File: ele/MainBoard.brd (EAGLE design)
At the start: 136.6 x 100 mm, 114 parts, among them IC1 MCP23017SP, IC2 74HC595D, IC3 74HC595D, X1 POWER_IN, X2 POWER_OUT

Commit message: ele: MainBoard - add description texts on PCB
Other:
- board text added: "!SLEEP"
- board text added: "+3V3"
- board text added: "H1"
- board text added: "H2"
- board text added: "H3"
- board text added: "H4"
- board text added: "HREF"
- board text added: "IN1"
- board text added: "IN2"
- board text added: "IN3"
- board text added: "IN4"
- board text added: "LREF"
- board text added: "OUT1"
- board text added: "OUT2"
- board text added: "OUT3"
- board text added: "OUT4"
- board text added: "VCC"
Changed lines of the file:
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@@
 <?xml version="1.0" encoding="utf-8"?>
 <!DOCTYPE eagle SYSTEM "eagle.dtd">
-<eagle version="9.0.1">
+<eagle version="9.0.0">
 <drawing>
 <settings>
@@
 <setting verticaltext="up"/>
 </settings>
-<grid distance="0.025" unitdist="inch" unit="mm" style="lines" multiple="1" display="yes" altdistance="0.01" altunitdist="inch" altunit="mm"/>
+<grid distance="0.025" unitdist="inch" unit="mil" style="lines" multiple="1" display="yes" altdistance="0.01" altunitdist="inch" altunit="mil"/>
 <layers>
 <layer number="1" name="Top" color="4" fill="1" visible="yes" active="yes"/>
@@
 <layer number="16" name="Bottom" color="1" fill="1" visible="yes" active="yes"/>
 <layer number="17" name="Pads" color="2" fill="1" visible="yes" active="yes"/>
-<layer number="18" name="Vias" color="2" fill="1" visible="no" active="yes"/>
+<layer number="18" name="Vias" color="2" fill="1" visible="yes" active="yes"/>
 <layer number="19" name="Unrouted" color="6" fill="1" visible="yes" active="yes"/>
 <layer number="20" name="Dimension" color="24" fill="1" visible="yes" active="yes"/>
@@
 <text x="15.751" y="51.562" size="1.5" layer="51" font="vector" ratio="20" rot="R270">M6</text>
 <text x="13.084" y="51.562" size="1.5" layer="51" font="vector" ratio="20" rot="R270">M5</text>
-<text x="19.688" y="7.239" size="1.5" layer="51" font="vector" ratio="20">IN</text>
+<text x="18.418" y="7.874" size="2.54" layer="51" font="vector" ratio="20">IN</text>
 <text x="12.319" y="95.885" size="1" layer="51" font="vector" ratio="20" rot="R270">SCL</text>
 <text x="2.156" y="23.114" size="1.5" layer="51" font="vector" ratio="20" rot="R90">M1</text>
@@
 <text x="27.559" y="4.445" size="1" layer="51" font="vector" ratio="20" rot="R270" align="bottom-right">GND</text>
 <text x="30.099" y="4.445" size="1" layer="51" font="vector" ratio="20" rot="R270" align="bottom-right">3V3</text>
-<text x="17.783" y="91.059" size="1.5" layer="51" font="vector" ratio="20">OUT</text>
+<text x="26.038" y="89.154" size="2.54" layer="51" font="vector" ratio="20">OUT</text>
 <text x="36.198" y="98.298" size="1.5" layer="51" font="vector" ratio="20">-</text>
 <text x="41.278" y="98.298" size="1.5" layer="51" font="vector" ratio="20">+</text>
@@
 <rectangle x1="45.818621875" y1="94.646221875" x2="46.631421875" y2="94.656378125" layer="21" rot="R90"/>
 <text x="53.975" y="72.39" size="1.4224" layer="21" font="vector" ratio="20" rot="R90">RobotikaBrno.cz</text>
+<text x="33.525" y="1.651" size="1.5" layer="51" font="vector" ratio="20" rot="R180">+</text>
+<text x="46.225" y="1.651" size="1.5" layer="51" font="vector" ratio="20" rot="R180">-</text>
+<text x="32.388" y="98.298" size="1.5" layer="51" font="vector" ratio="20">-</text>
+<text x="45.723" y="98.298" size="1.5" layer="51" font="vector" ratio="20">+</text>
+<text x="49.801" y="40.894" size="1" layer="51" font="vector" ratio="20">EN</text>
+<text x="49.801" y="43.434" size="1" layer="51" font="vector" ratio="20">IN</text>
+<text x="49.801" y="45.974" size="1" layer="51" font="vector" ratio="20">GND</text>
+<text x="49.801" y="48.514" size="1" layer="51" font="vector" ratio="20">OUT</text>
+<text x="128.668" y="30.099" size="1" layer="51" font="vector" ratio="20">EN</text>
+<text x="128.668" y="25.019" size="1" layer="51" font="vector" ratio="20">IN</text>
+<text x="128.668" y="27.559" size="1" layer="51" font="vector" ratio="20">GND</text>
+<text x="128.668" y="22.479" size="1" layer="51" font="vector" ratio="20">OUT</text>
+<text x="128.795" y="75.819" size="1" layer="51" font="vector" ratio="20">EN</text>
+<text x="128.795" y="70.739" size="1" layer="51" font="vector" ratio="20">IN</text>
+<text x="128.795" y="73.279" size="1" layer="51" font="vector" ratio="20">GND</text>
+<text x="128.795" y="68.199" size="1" layer="51" font="vector" ratio="20">OUT</text>
+<text x="41.546" y="12.319" size="1" layer="51" font="vector" ratio="20">IN1</text>
+<text x="41.546" y="14.859" size="1" layer="51" font="vector" ratio="20">IN2</text>
+<text x="41.546" y="17.399" size="1" layer="51" font="vector" ratio="20">VCC</text>
+<text x="41.546" y="19.939" size="1" layer="51" font="vector" ratio="20">GND</text>
+<text x="41.546" y="22.479" size="1" layer="51" font="vector" ratio="20">IN3</text>
+<text x="41.546" y="25.019" size="1" layer="51" font="vector" ratio="20">IN4</text>
+<text x="41.546" y="32.639" size="1" layer="51" font="vector" ratio="20">IN1</text>
+<text x="41.546" y="35.179" size="1" layer="51" font="vector" ratio="20">IN2</text>
+<text x="41.546" y="37.719" size="1" layer="51" font="vector" ratio="20">VCC</text>
+<text x="41.546" y="40.259" size="1" layer="51" font="vector" ratio="20">GND</text>
+<text x="41.546" y="42.799" size="1" layer="51" font="vector" ratio="20">IN3</text>
+<text x="41.546" y="45.339" size="1" layer="51" font="vector" ratio="20">IN4</text>
+<text x="41.546" y="52.959" size="1" layer="51" font="vector" ratio="20">IN1</text>
+<text x="41.546" y="55.499" size="1" layer="51" font="vector" ratio="20">IN2</text>
+<text x="41.546" y="58.039" size="1" layer="51" font="vector" ratio="20">VCC</text>
+<text x="41.546" y="60.579" size="1" layer="51" font="vector" ratio="20">GND</text>
+<text x="41.546" y="63.119" size="1" layer="51" font="vector" ratio="20">IN3</text>
+<text x="41.546" y="65.659" size="1" layer="51" font="vector" ratio="20">IN4</text>
+<text x="41.546" y="73.279" size="1" layer="51" font="vector" ratio="20">IN1</text>
+<text x="41.546" y="75.819" size="1" layer="51" font="vector" ratio="20">IN2</text>
+<text x="41.546" y="78.359" size="1" layer="51" font="vector" ratio="20">VCC</text>
+<text x="41.546" y="80.899" size="1" layer="51" font="vector" ratio="20">GND</text>
+<text x="41.546" y="83.439" size="1" layer="51" font="vector" ratio="20">IN3</text>
+<text x="41.546" y="85.979" size="1" layer="51" font="vector" ratio="20">IN4</text>
+<text x="25.671" y="12.319" size="1" layer="51" font="vector" ratio="20">!FAULT</text>
+<text x="25.671" y="14.859" size="1" layer="51" font="vector" ratio="20">OUT4</text>
+<text x="25.671" y="17.399" size="1" layer="51" font="vector" ratio="20">OUT3</text>
+<text x="25.671" y="19.939" size="1" layer="51" font="vector" ratio="20">OUT2</text>
+<text x="25.671" y="22.479" size="1" layer="51" font="vector" ratio="20">OUT1</text>
+<text x="25.671" y="25.019" size="1" layer="51" font="vector" ratio="20">!SLEEP</text>
+<text x="25.671" y="32.639" size="1" layer="51" font="vector" ratio="20">!FAULT</text>
+<text x="25.671" y="35.179" size="1" layer="51" font="vector" ratio="20">OUT4</text>
+<text x="25.671" y="37.719" size="1" layer="51" font="vector" ratio="20">OUT3</text>
+<text x="25.671" y="40.259" size="1" layer="51" font="vector" ratio="20">OUT2</text>
+<text x="25.671" y="42.799" size="1" layer="51" font="vector" ratio="20">OUT1</text>
+<text x="25.671" y="45.339" size="1" layer="51" font="vector" ratio="20">!SLEEP</text>
+<text x="25.671" y="52.959" size="1" layer="51" font="vector" ratio="20">!FAULT</text>
+<text x="25.671" y="55.499" size="1" layer="51" font="vector" ratio="20">OUT4</text>
+<text x="25.671" y="58.039" size="1" layer="51" font="vector" ratio="20">OUT3</text>
+<text x="25.671" y="60.579" size="1" layer="51" font="vector" ratio="20">OUT2</text>
+<text x="25.671" y="63.119" size="1" layer="51" font="vector" ratio="20">OUT1</text>
+<text x="25.671" y="65.659" size="1" layer="51" font="vector" ratio="20">!SLEEP</text>
+<text x="25.671" y="73.279" size="1" layer="51" font="vector" ratio="20">!FAULT</text>
+<text x="25.671" y="75.819" size="1" layer="51" font="vector" ratio="20">OUT4</text>
+<text x="25.671" y="78.359" size="1" layer="51" font="vector" ratio="20">OUT3</text>
+<text x="25.671" y="80.899" size="1" layer="51" font="vector" ratio="20">OUT2</text>
+<text x="25.671" y="83.439" size="1" layer="51" font="vector" ratio="20">OUT1</text>
+<text x="25.671" y="85.979" size="1" layer="51" font="vector" ratio="20">!SLEEP</text>
+<text x="89.298" y="33.02" size="1" layer="51" font="vector" ratio="20">H1</text>
+<text x="89.298" y="35.56" size="1" layer="51" font="vector" ratio="20">H2</text>
+<text x="89.298" y="38.1" size="1" layer="51" font="vector" ratio="20">HREF</text>
+<text x="89.298" y="40.64" size="1" layer="51" font="vector" ratio="20">GND</text>
+<text x="89.298" y="43.18" size="1" layer="51" font="vector" ratio="20">H3</text>
+<text x="89.298" y="45.72" size="1" layer="51" font="vector" ratio="20">H4</text>
+<text x="96.283" y="33.02" size="1" layer="51" font="vector" ratio="20" align="bottom-right">L1</text>
+<text x="96.283" y="35.56" size="1" layer="51" font="vector" ratio="20" align="bottom-right">L2</text>
+<text x="96.283" y="38.1" size="1" layer="51" font="vector" ratio="20" align="bottom-right">LREF</text>
+<text x="96.283" y="40.64" size="1" layer="51" font="vector" ratio="20" align="bottom-right">GND</text>
+<text x="96.283" y="43.18" size="1" layer="51" font="vector" ratio="20" align="bottom-right">L3</text>
+<text x="96.283" y="45.72" size="1" layer="51" font="vector" ratio="20" align="bottom-right">L4</text>
+<text x="52.708" y="98.298" size="1.5" layer="51" font="vector" ratio="20">-</text>
+<text x="111.128" y="98.298" size="1.5" layer="51" font="vector" ratio="20">-</text>
+<text x="102.873" y="98.298" size="1.5" layer="51" font="vector" ratio="20">+3V3</text>
 </plain>
 <attributes>
@@
 <vertex x="46.99" y="7.62"/>
 </polygon>
+<wire x1="41.91" y1="93.599" x2="39.23" y2="78.74" width="0" layer="19" extent="1-1"/>
+<wire x1="39.23" y1="17.78" x2="36.83" y2="5.461" width="0" layer="19" extent="1-1"/>
+<wire x1="39.23" y1="38.1" x2="53.975" y2="43.815" width="0" layer="19" extent="1-1"/>
+<wire x1="39.23" y1="58.42" x2="39.23" y2="78.74" width="0" layer="19" extent="1-1"/>
 </signal>
 <signal name="EN">

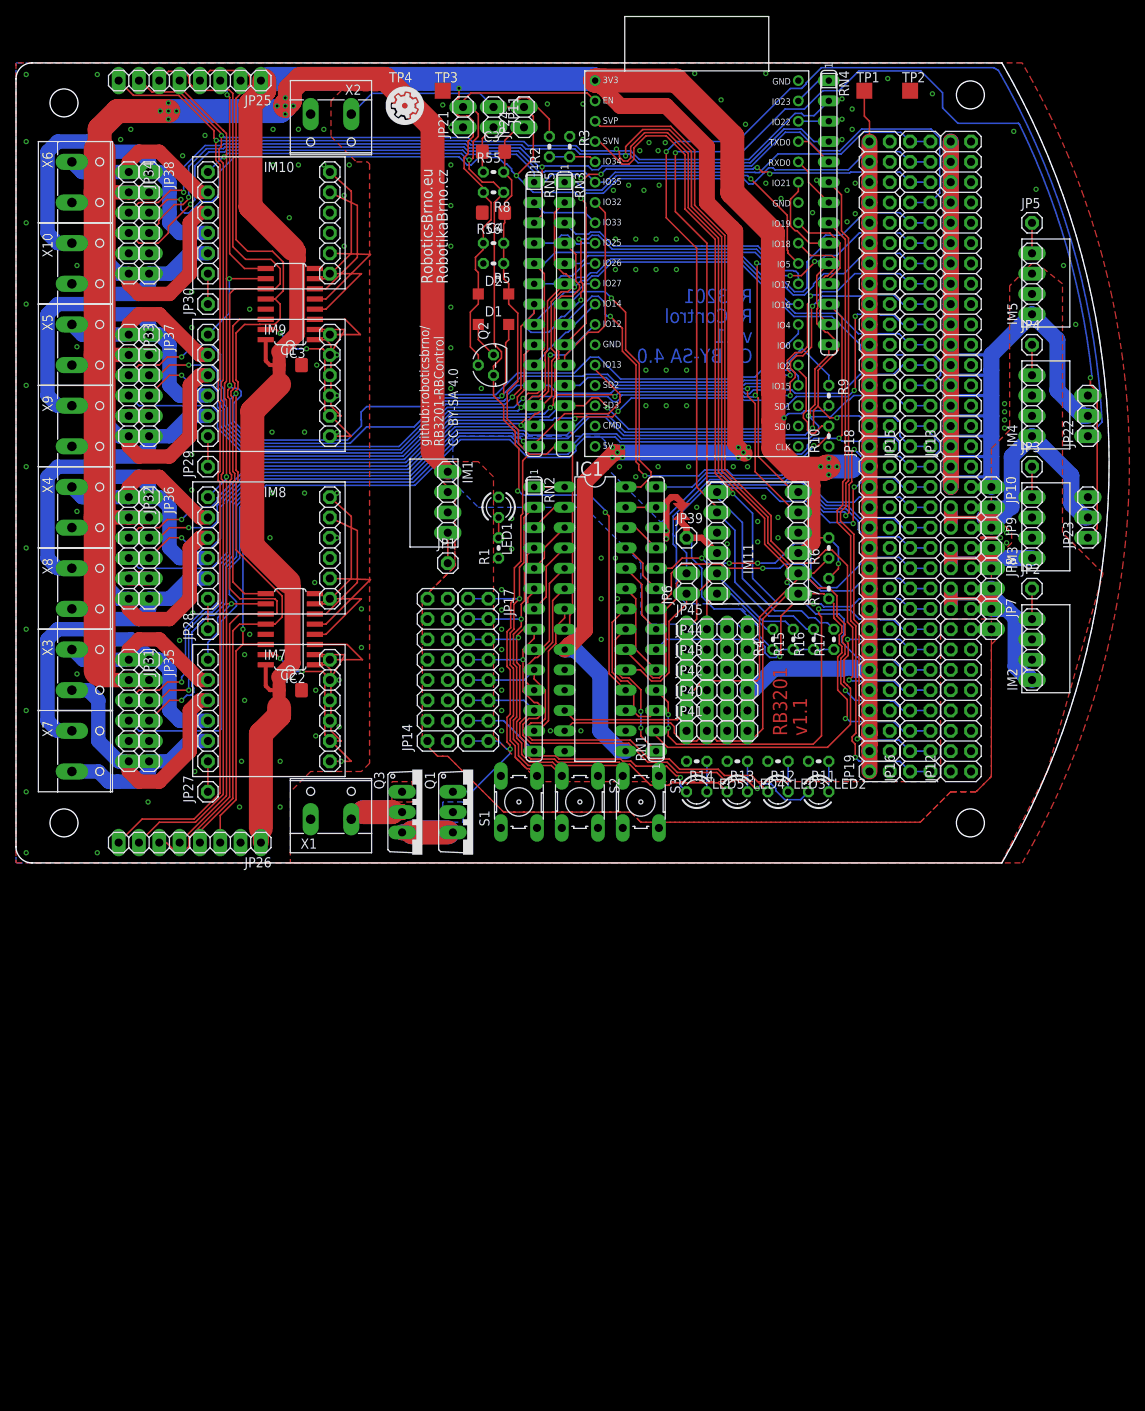
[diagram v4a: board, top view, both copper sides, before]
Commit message: ele: move power switch from GND to VCC (schematic only)
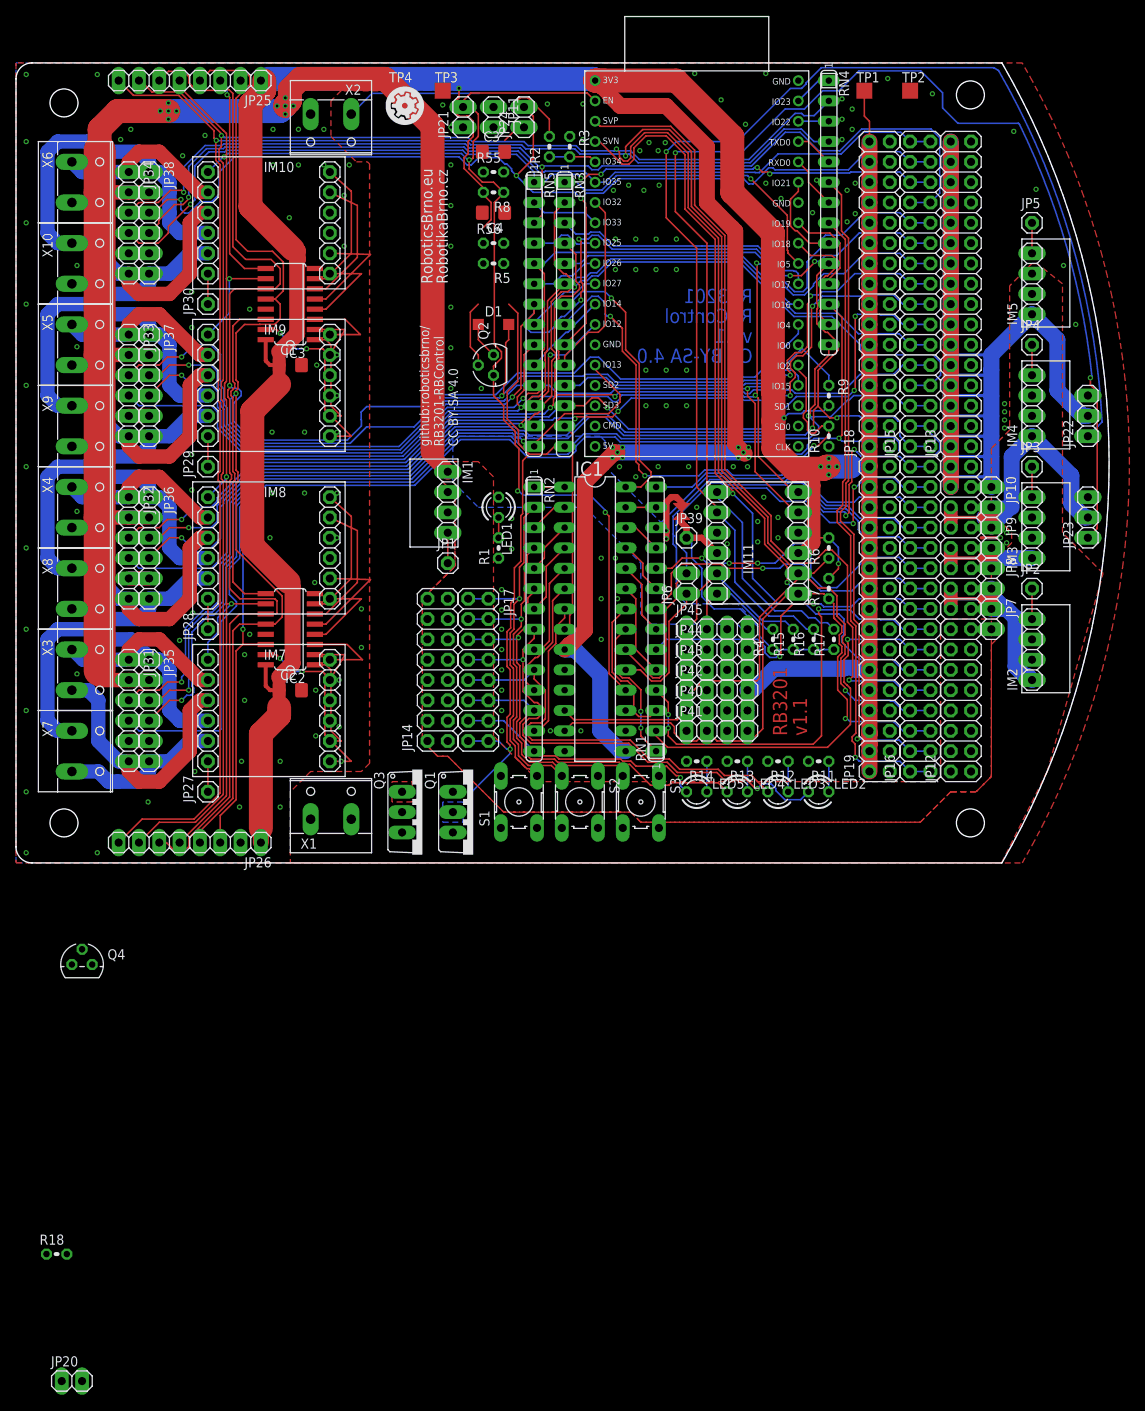
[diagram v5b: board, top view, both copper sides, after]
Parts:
- removed D2: (no value), diode:SOD123
- added JP20: STOP_BUTTON, pinhead:1X02
- added Q4: (no value), transistors:TO92
- added R18: 2M, rcl_upravena:0204V
- JP11: value POWER_BUTTON -> START_BUTTON
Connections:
- removed net BATT_CATHODE: Q3.2, X1.2
- removed net BATT_CATHODE2: Q1.3, Q3.3
- removed net N$19: C3.1, JP11.2, R55.1
- new net BAT: Q3.2, X1.1
- new net BAT_PROT: Q1.3, Q3.3, R5.1
- new net N$1: C3.1, Q1.1, Q4.3, R18.1, R5.2
- new net N$6: C3.2, JP11.1, R18.2
- net +3V3: no longer D2.C
- net ESP_!SHUTDOWN: now also JP20.1, Q4.2, R55.1; no longer C3.2, D2.A, Q1.1, R5.1, R55.2
- net GND: now also JP11.2, JP20.2, Q3.1, Q4.1, R55.2, X1.2; no longer Q1.2, R5.2
- net VCC: now also Q1.2; no longer JP11.1, Q3.1, X1.1
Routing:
- net ESP_!SHUTDOWN: track 104.3 -> 80.4 mm
- net BATT_CATHODE: track 13.4 -> 0.00 mm
- net BATT_CATHODE2: track 12.7 -> 0.00 mm
- net +3V3: track 543.4 -> 533.2 mm
- net N$19: track 6.22 -> 0.00 mm
- net VCC: track 30.3 -> 25.7 mm

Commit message: ele: Fix layout on left side (motor drivers)
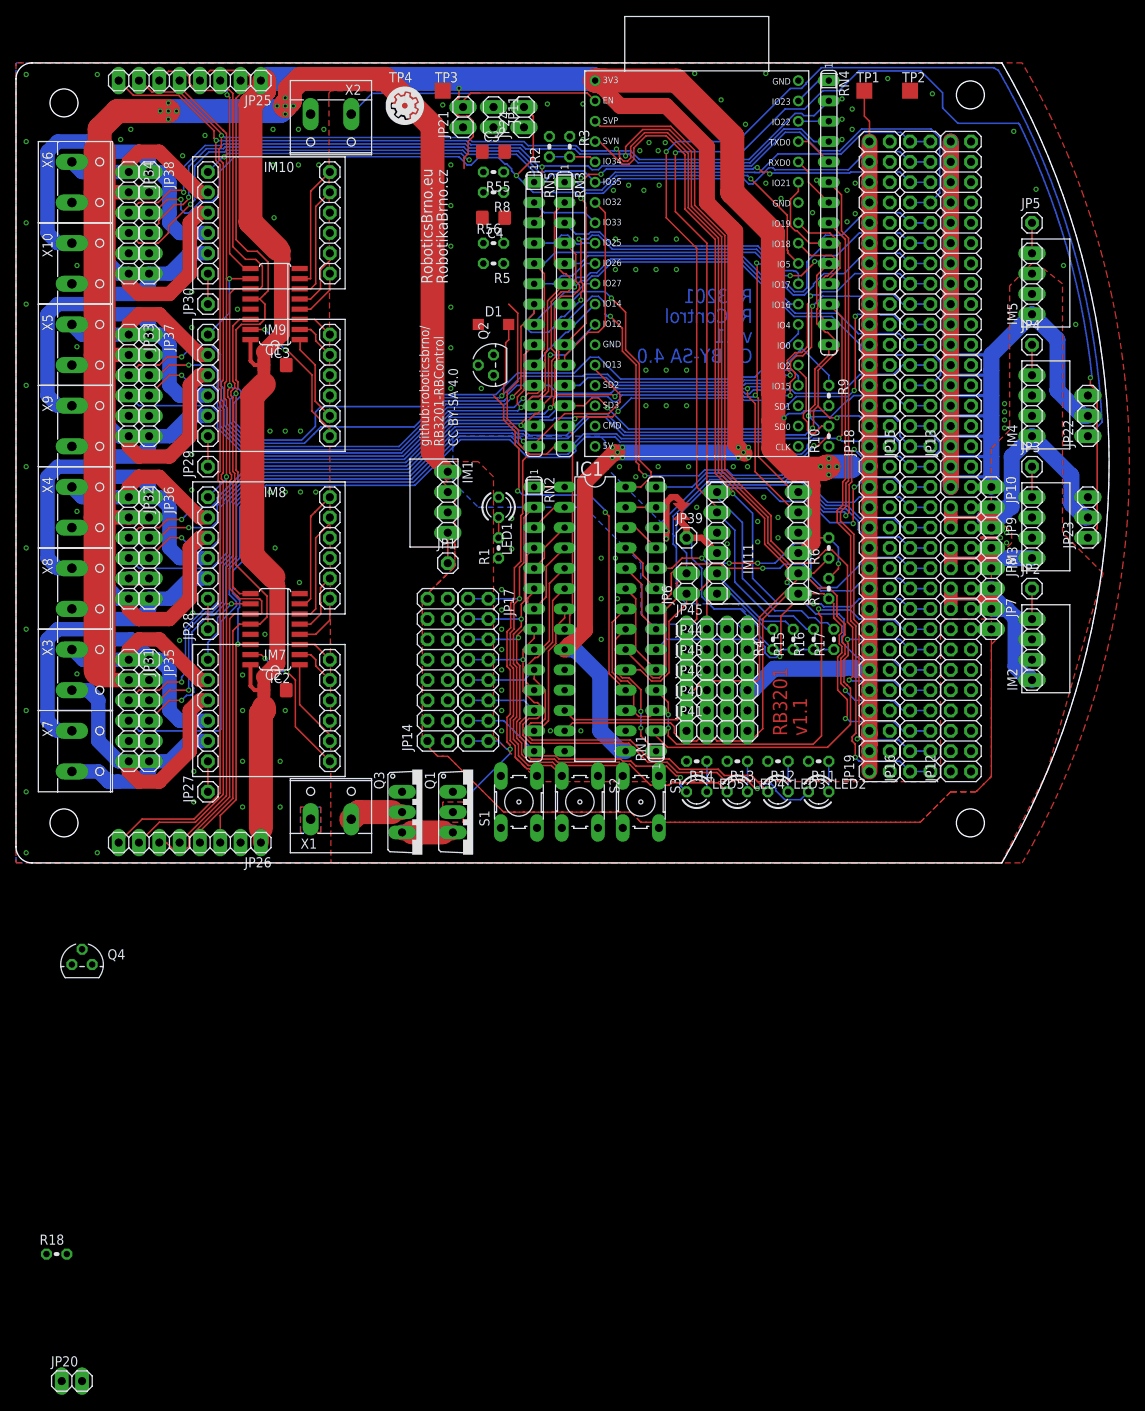
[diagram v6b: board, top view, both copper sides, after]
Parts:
- moved C1 1.91 mm to (32.4, 62.2)
- moved C2 1.91 mm to (32.4, 21.6)
- moved IC2 1.91 mm to (32.4, 29.2)
- moved IC3 1.91 mm to (32.4, 69.8)
- moved C4 0.64 mm to (59.7, 80.6)
- turned R55 to 180 degrees
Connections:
- net BAT: now also X1.2; no longer X1.1
- net GND: now also X1.1; no longer X1.2
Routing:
- net EN: track 273.6 -> 228.1 mm
- net +3V3: track 533.2 -> 512.9 mm
- net VCC: track 25.7 -> 17.1 mm
- net SCKMOT: track 219.9 -> 212.3 mm
- net BAT: track 0.00 -> 6.72 mm
- net BAT_PROT: track 0.00 -> 6.35 mm
- net RCKMOT: track 222.9 -> 216.6 mm
- net IC3_F: track 14.3 -> 8.08 mm
- net IC2_D: track 10.8 -> 4.56 mm
- net IC2_F: track 14.3 -> 8.11 mm
- net IC3_D: track 10.3 -> 4.56 mm
- net IC3_E: track 11.6 -> 6.81 mm
- net _EN_: track 4.60 -> 0.00 mm
- net IC3_A: track 23.2 -> 18.6 mm
- net IC2_A: track 23.4 -> 18.9 mm
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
